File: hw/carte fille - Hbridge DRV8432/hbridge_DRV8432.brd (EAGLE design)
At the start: 50 x 40 mm, 37 parts, among them IC1 DRV8402

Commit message: Start routing the board
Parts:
- moved R1 28.1 mm to (-8.89, 27.9)
- moved C16 18.0 mm to (60.2, 19.6)
- moved C19 17.8 mm to (60.2, 14.0)
- moved R3 17.8 mm to (-11.4, 24.1)
- moved C20 17.7 mm to (59.7, 29.7)
- moved C15 16.9 mm to (58.9, 25.4)
- moved R2 16.1 mm to (-7.87, 20.3), turned to 0 degrees
- moved R11 14.0 mm to (-7.62, 16.5)
- moved C18 14.0 mm to (24.1, 4.57), turned to 270 degrees
- moved R4 8.52 mm to (11.9, 17.3), turned to 225 degrees
- moved R7 7.47 mm to (13.5, 15.7), turned to 225 degrees
- moved R8 6.65 mm to (15.0, 14.2), turned to 225 degrees
- moved C2 6.49 mm to (19.6, 10.7), turned to 270 degrees
- moved C7 5.73 mm to (21.6, 10.7), turned to 270 degrees
- moved R9 4.60 mm to (15.0, 20.8)
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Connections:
- net GND: no longer C15.1, C16.1, C19.1, C20.1
- net GVDD: no longer R1.2, R11.2, R2.2, R3.2
- net N$1: no longer R3.1
- net N$16: now also IC1.P$5; no longer IC1.P$15, R11.1
- net N$17: now also IC1.P$6; no longer IC1.P$4
- net N$18: now also IC1.P$14; no longer IC1.P$6
- net N$19: now also IC1.P$15; no longer IC1.P$14
- net N$6: no longer R2.1
- net N$8: now also IC1.P$4; no longer IC1.P$5, R1.1
- net PVDD: no longer C15.2, C16.2, C19.2, C20.2
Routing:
- net PVDD: track 0.00 -> 96.0 mm, vias 0 -> 4
- net GVDD: track 0.00 -> 83.7 mm
- net N$17: track 0.00 -> 21.9 mm
- net N$16: track 0.00 -> 20.5 mm
- net N$20: track 0.00 -> 20.2 mm
- net N$19: track 0.00 -> 19.4 mm
- net N$8: track 0.00 -> 19.2 mm
- net N$18: track 0.00 -> 18.6 mm
- net N$6: track 0.00 -> 18.4 mm
- net N$1: track 0.00 -> 17.8 mm
- net GND: track 0.00 -> 16.4 mm, vias 0 -> 3
- net OUT_D: track 0.00 -> 10.8 mm
- net N$5: track 0.00 -> 10.4 mm
- net OUT_C: track 0.00 -> 10.0 mm
- net OUT_A: track 0.00 -> 9.84 mm
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- added copper zone on layer 1, net GND
- added copper zone on layer 16, net GND

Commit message: rework board routing
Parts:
- removed C10, C11, C12, C13, C15, C16, C19, C20: 100nF - 0805, resistor:C0805
- removed C14: 100n, etienne:805
- removed C18: 47uF, etienne:E3,5-8
- removed C22: 330µF, etienne:E3,5-8
- removed C5: 10nF - 0805, resistor:C0805
- removed SIGNAL: (no value), con-lsta:FE09
- added C17: 47u, rcl:B/3528-21W
- added C21: 1u, rcl:C0805
- added C31, C32, C33, C34: 100n, rcl:C0805
- added C35, C36, C37, C38: 100n, rcl:C0603
- added H1, H2, H3, H4: MOUNT-HOLE3.2, holes:3,2
- added JP1: (no value), pinhead-2:1X08
- added X4: M1-2, con-wago-500:W237-102
- added X5: M3-4, con-wago-500:W237-102
- added X6: +12V, con-wago-500:W237-102
- added X7: +24V, con-wago-500:W237-102
- C1: value 10nF - 0805 -> 10n; device resistor:C0805 -> rcl:C0805
- C2, C6, C8: value 1uF - 0805 -> 1u; device resistor:C0805 -> rcl:C0805
- C3: value 1000uF -> 1000u; device etienne:E3,5-8 -> rcl:E3,5-10
- C4: value 1000uF -> 100n; device etienne:E3,5-8 -> rcl:C0603K
- C7: value 1uF -0805 -> 1u; device resistor:C0805 -> rcl:C0805
- C9: value 1uF - 0805 -> 330u; device resistor:C0805 -> rcl:B/3528-21W
- R10: value 3R3 - 0603 -> 3.3; device resistor:R0603 -> rcl:R1206
- R12: value 3R3 - 0603 -> (none); device resistor:R0603 -> rcl:R0603
- R9: value 27K - 0603 -> 1; device resistor:R0603 -> rcl:R0603
- moved X1 38.4 mm to (41.1, 19.6), turned to 270 degrees
- moved R12 35.0 mm to (9.04, 18.7)
- moved R5 32.8 mm to (37.6, 18.4), turned to 180 degrees
- moved C9 30.5 mm to (10.2, 27.9)
- moved R6 29.9 mm to (37.6, 23.4), turned to 180 degrees
- moved C4 27.9 mm to (12.8, 19.0), turned to 90 degrees
- moved X2 23.6 mm to (21.9, 31.2), turned to 180 degrees
- moved X3 23.4 mm to (21.9, 7.85), turned to 0 degrees
- moved C8 20.9 mm to (10.0, 11.0)
- moved C2 20.9 mm to (29.8, 28.8), turned to 180 degrees
- moved C6 19.2 mm to (29.6, 10.1), turned to 180 degrees
- moved R11 12.5 mm to (-13.2, 27.7)
- moved R2 10.8 mm to (-15.7, 27.7), turned to 90 degrees
- moved R10 8.00 mm to (34.3, 31.5)
- moved C7 6.93 mm to (14.7, 10.8), turned to 90 degrees
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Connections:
- removed net N$14: C5.1, R12.2
- removed net N$15: C13.1, IC1.P$35
- removed net N$22: R5.1, X1.3
- removed net OUT_A: C13.2, IC1.P$33, X2.1
- removed net OUT_B: C12.2, IC1.P$30, X2.2
- removed net OUT_C: C11.2, IC1.P$25, X3.1
- removed net OUT_D: C10.2, IC1.P$22, X3.2
- new net GND1: X6.1, X7.1
- new net M1A: C33.1, IC1.P$33, X2.1, X4.1
- new net M1B: C32.1, IC1.P$30, X2.2, X4.2
- new net M1C: C31.2, IC1.P$25, X3.1, X5.1
- new net M1D: C34.2, IC1.P$22, X3.2, X5.2
- new net N$25: C33.2, IC1.P$35
- new net N$26: C32.2, IC1.P$28
- new net N$27: C31.1, IC1.P$27
- new net N$28: C34.1, IC1.P$20
- net GND: now also C1.1, C17.-, C2.1, C21.1, C35.1, C36.1, C37.1, C38.1, C6.1, C7.1, C8.1, C9.-, R9.1, X1.4; no longer C1.2, C14.1, C18.-, C2.2, C22.-, C4.-, C5.2, C6.2, C7.2, C8.2, C9.2, IC1.P$9, R4.2, R7.2, R8.2, R9.2, SIGNAL.1, X1.1
- net GVDD: now also C17.+, C2.2, C21.2, C6.2, C7.2, C8.2, C9.+; no longer C18.+, C2.1, C22.+, C6.1, C7.1, C8.1, C9.1
- net N$1: now also JP1.8; no longer SIGNAL.9
- net N$10: now also IC1.P$7, R12.2; no longer C12.1, IC1.P$28
- net N$11: now also C4.1; no longer C14.2
- net N$12: now also X1.2; no longer C10.1, IC1.P$20
- net N$13: now also C1.2, R10.1; no longer C1.1, R10.2
- net N$16: now also JP1.5; no longer SIGNAL.6
- net N$17: now also JP1.4; no longer SIGNAL.5
- net N$18: now also JP1.3; no longer SIGNAL.4
- net N$19: now also JP1.2; no longer SIGNAL.3
- net N$2: now also X1.1, X6.2; no longer X1.2
- net N$20: now also JP1.1; no longer SIGNAL.2
- net N$6: now also JP1.7; no longer SIGNAL.8
- net N$7: now also R5.1, X1.3, X7.2; no longer C11.1, IC1.P$27
- net N$8: now also JP1.6; no longer SIGNAL.7
- net N$9: now also C4.2, IC1.P$9, R12.1, R4.2, R7.2, R8.2, R9.2; no longer IC1.P$7, R9.1
- net PVDD: now also C35.2, C36.2, C37.2, C38.2, R10.2; no longer C4.+, R10.1, R12.1
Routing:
- net PVDD: track 96.0 -> 13.2 mm, vias 4 -> 0
- net N$26: track 0.00 -> 25.4 mm
- net N$27: track 0.00 -> 24.4 mm
- net M1D: track 0.00 -> 20.9 mm
- net M1C: track 0.00 -> 20.8 mm
- net M1B: track 0.00 -> 19.2 mm
- net M1A: track 0.00 -> 18.0 mm
- net OUT_D: track 10.8 -> 0.00 mm
- net N$25: track 0.00 -> 10.6 mm
- net OUT_C: track 10.0 -> 0.00 mm
- net OUT_A: track 9.84 -> 0.00 mm
- net OUT_B: track 9.69 -> 0.00 mm
- net GVDD: track 83.7 -> 91.6 mm
- net N$17: track 21.9 -> 14.1 mm
- net GND: track 16.4 -> 8.88 mm, vias 3 -> 0
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- added copper zone on layer 1, net M1A
- added copper zone on layer 1, net M1B
- added copper zone on layer 1, net M1C
- added copper zone on layer 1, net M1D
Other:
- board size 50 x 40 mm -> 50 x 39 mm

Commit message: wip
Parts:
- removed R5, R6: 0R, resistor:R0603
- moved R9 1.14 mm to (10.1, 19.2)
- moved R12 1.10 mm to (8.05, 19.2)
- moved C4 0.42 mm to (12.5, 18.7)
- moved R10 0.25 mm to (34.1, 31.3)
- moved C37 0.22 mm to (34.1, 13.8), turned to 90 degrees
- moved C1 0.22 mm to (36.4, 33.7)
- moved C36 0.20 mm to (34.1, 25.4), turned to 270 degrees
- moved C38 0.13 mm to (32.0, 13.8), turned to 90 degrees
- turned C35 to 270 degrees
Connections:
- removed net GND1: X6.1, X7.1
- removed net N$2: R6.1, X1.1, X6.2
- removed net N$7: R5.1, X1.3, X7.2
- net GND: now also X6.1, X7.1
- net GVDD: now also X1.1, X6.2; no longer R6.2
- net PVDD: now also X1.3, X7.2; no longer R5.2
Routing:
- net PVDD: track 13.2 -> 67.1 mm
- net GVDD: track 91.6 -> 135.3 mm
- net N$9: track 2.27 -> 19.7 mm, vias 0 -> 1
- net N$28: track 0.00 -> 11.2 mm
- net GND: track 8.88 -> 18.7 mm, vias 0 -> 3
- net N$2: track 9.24 -> 0.00 mm
- net N$7: track 8.01 -> 0.00 mm
- net N$13: track 2.29 -> 3.33 mm
- net N$4: track 6.01 -> 4.99 mm
- net N$3: track 6.60 -> 5.58 mm
- net N$5: track 6.52 -> 5.51 mm
- net N$11: track 2.73 -> 3.55 mm
- net N$10: track 6.63 -> 7.42 mm
- net N$26: track 25.4 -> 24.9 mm
- added copper zone on layer 1, net PVDD
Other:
- board size 50 x 39 mm -> 53.6 x 42 mm

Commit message: finish routing
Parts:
- removed R1, R11, R2, R3: 10K - 0603, resistor:R0603
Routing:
- net M1C: track 20.8 -> 26.9 mm
- net M1B: track 19.2 -> 24.5 mm
- net PVDD: track 67.1 -> 70.1 mm
- net M1A: track 18.0 -> 20.6 mm
- net M1D: track 20.9 -> 22.9 mm
- net GVDD: track 135.3 -> 136.1 mm
- removed copper zone on layer 1, net M1A
- removed copper zone on layer 1, net M1B
- removed copper zone on layer 1, net M1C
- removed copper zone on layer 1, net M1D
- removed copper zone on layer 1, net PVDD

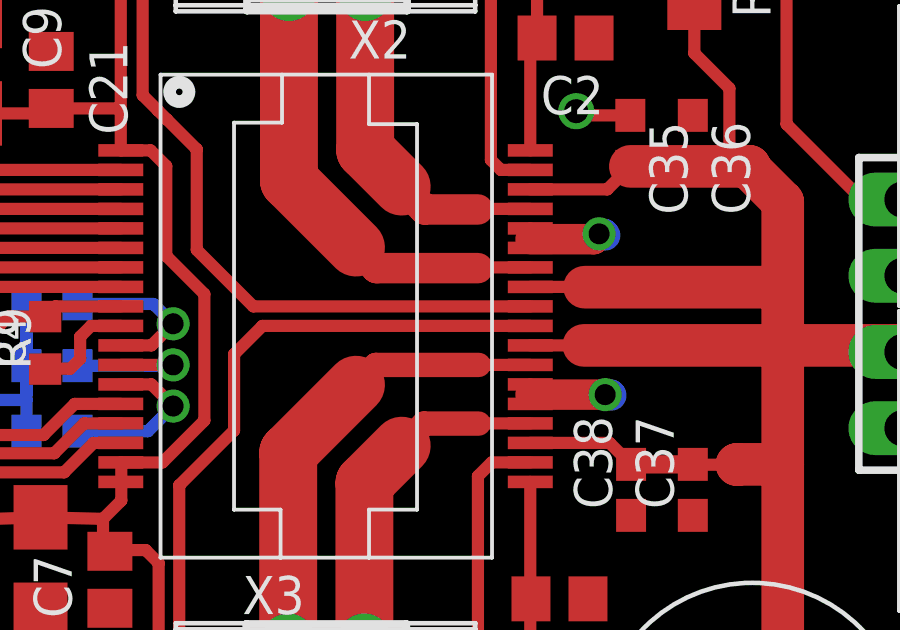
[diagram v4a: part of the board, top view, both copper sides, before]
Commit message: fix power section
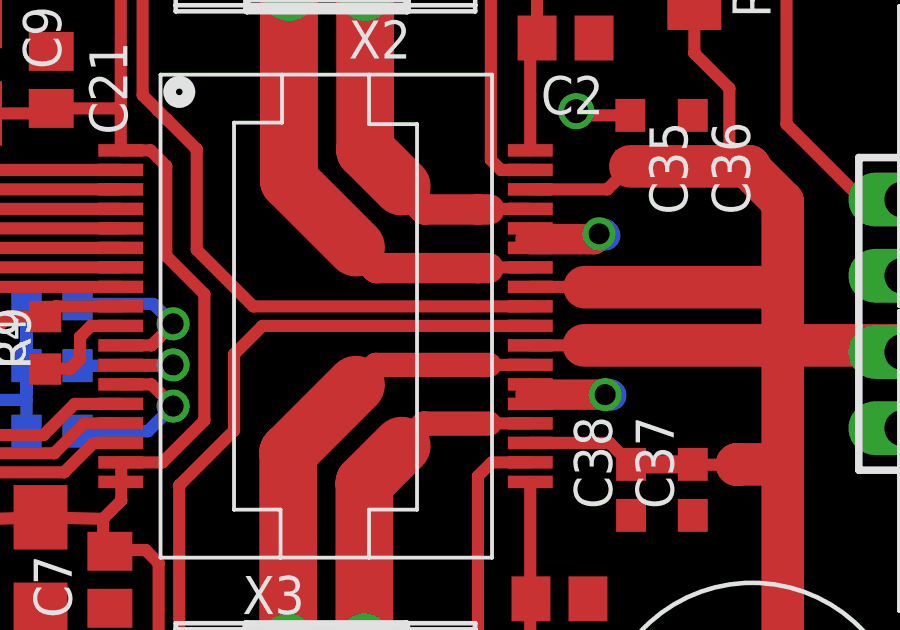
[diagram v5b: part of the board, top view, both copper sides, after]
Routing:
- net M1C: track 26.9 -> 27.6 mm
- net M1B: track 24.5 -> 25.2 mm
- net M1D: track 22.9 -> 23.6 mm
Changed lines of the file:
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@@
 <wire x1="23.1648" y1="31.1912" x2="23.1648" y2="25.0952" width="1.9304" layer="1"/>
 <wire x1="23.1648" y1="25.0952" x2="24.384" y2="23.876" width="1.9304" layer="1"/>
-<wire x1="28.669" y1="23.133" x2="26.943" y2="23.133" width="0.4064" layer="1"/>
-<wire x1="26.943" y1="23.133" x2="26.924" y2="23.114" width="0.4064" layer="1"/>
+<wire x1="27.305" y1="23.114" x2="26.924" y2="23.114" width="1.016" layer="1"/>
 <wire x1="26.924" y1="23.114" x2="25.146" y2="23.114" width="1.016" layer="1"/>
 <wire x1="25.146" y1="23.114" x2="24.384" y2="23.876" width="1.016" layer="1"/>
-<wire x1="27.0002" y1="23.114" x2="27.0002" y2="23.0886" width="0.6096" layer="1"/>
+<wire x1="26.924" y1="23.114" x2="27.0002" y2="23.0886" width="0.6096" layer="1"/>
 <wire x1="27.0002" y1="23.0886" x2="26.9748" y2="23.0632" width="0.6096" layer="1"/>
-<wire x1="27.0002" y1="23.114" x2="26.924" y2="23.114" width="0.6096" layer="1"/>
+<wire x1="28.669" y1="23.133" x2="27.305" y2="23.133" width="0.4064" layer="1"/>
+<wire x1="27.305" y1="23.133" x2="27.305" y2="23.114" width="0.4064" layer="1"/>
 </signal>
 <signal name="M1B">
@@
 <wire x1="20.6248" y1="31.1912" x2="20.6248" y2="24.0792" width="1.9304" layer="1"/>
 <wire x1="20.6248" y1="24.0792" x2="22.86" y2="21.844" width="1.9304" layer="1"/>
-<wire x1="28.669" y1="21.183" x2="26.9488" y2="21.183" width="0.4064" layer="1"/>
-<wire x1="26.9488" y1="21.183" x2="26.924" y2="21.1582" width="0.4064" layer="1"/>
+<wire x1="26.9488" y1="21.183" x2="27.2796" y2="21.1582" width="0.4064" layer="1"/>
+<wire x1="27.2796" y1="21.1582" x2="26.924" y2="21.1582" width="1.016" layer="1"/>
 <wire x1="26.924" y1="21.1582" x2="23.5458" y2="21.1582" width="1.016" layer="1"/>
 <wire x1="23.5458" y1="21.1582" x2="22.86" y2="21.844" width="1.016" layer="1"/>
+<wire x1="28.669" y1="21.183" x2="26.924" y2="21.183" width="0.4064" layer="1"/>
+<wire x1="26.924" y1="21.183" x2="26.924" y2="21.1582" width="0.4064" layer="1"/>
 </signal>
 <signal name="M1C">
@@
 <wire x1="20.5994" y1="15.0114" x2="22.86" y2="17.272" width="1.9304" layer="1"/>
 <wire x1="28.669" y1="17.933" x2="26.95" y2="17.933" width="0.4064" layer="1"/>
-<wire x1="26.95" y1="17.933" x2="26.9494" y2="17.9324" width="0.4064" layer="1"/>
-<wire x1="26.9494" y1="17.9324" x2="23.5204" y2="17.9324" width="0.8128" layer="1"/>
+<wire x1="26.95" y1="17.933" x2="27.305" y2="17.9324" width="0.4064" layer="1"/>
+<wire x1="27.305" y1="17.9324" x2="23.5204" y2="17.9324" width="0.8128" layer="1"/>
 <wire x1="23.5204" y1="17.9324" x2="22.86" y2="17.272" width="0.8128" layer="1"/>
 </signal>
@@
 <wire x1="23.1394" y1="13.9954" x2="24.384" y2="15.24" width="1.9304" layer="1"/>
 <wire x1="28.669" y1="15.983" x2="26.9558" y2="15.983" width="0.4064" layer="1"/>
-<wire x1="26.9558" y1="15.983" x2="26.9494" y2="15.9766" width="0.4064" layer="1"/>
-<wire x1="26.9494" y1="15.9766" x2="25.1206" y2="15.9766" width="0.8128" layer="1"/>
+<wire x1="26.9558" y1="15.983" x2="27.305" y2="15.9766" width="0.4064" layer="1"/>
+<wire x1="27.305" y1="15.9766" x2="25.1206" y2="15.9766" width="0.8128" layer="1"/>
 <wire x1="25.1206" y1="15.9766" x2="24.384" y2="15.24" width="0.8128" layer="1"/>
 </signal>

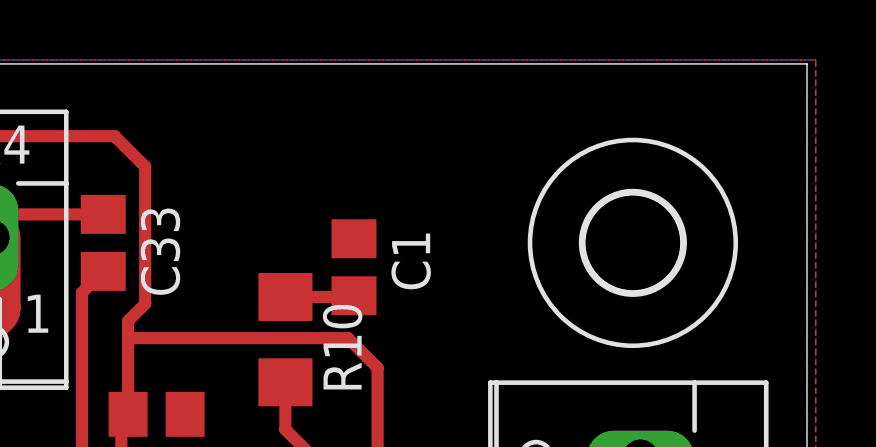
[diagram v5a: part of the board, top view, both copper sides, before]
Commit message: add open hardware logo
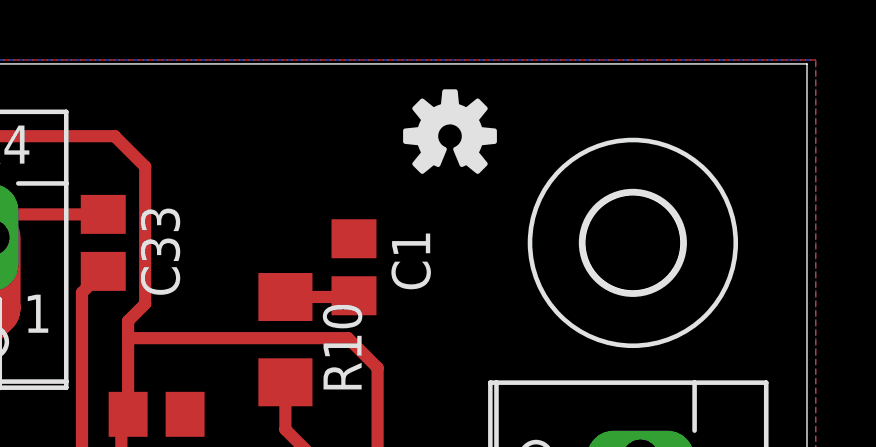
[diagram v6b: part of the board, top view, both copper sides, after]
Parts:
- added U$1: OSHW-LOGOS, SparkFun-Aesthetics:OSHW-LOGO-S
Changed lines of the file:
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@@
 <layer number="19" name="Unrouted" color="6" fill="1" visible="yes" active="yes"/>
 <layer number="20" name="Dimension" color="15" fill="1" visible="yes" active="yes"/>
-<layer number="21" name="tPlace" color="7" fill="1" visible="no" active="yes"/>
-<layer number="22" name="bPlace" color="7" fill="1" visible="no" active="yes"/>
+<layer number="21" name="tPlace" color="7" fill="1" visible="yes" active="yes"/>
+<layer number="22" name="bPlace" color="7" fill="1" visible="yes" active="yes"/>
 <layer number="23" name="tOrigins" color="15" fill="1" visible="yes" active="yes"/>
 <layer number="24" name="bOrigins" color="15" fill="1" visible="yes" active="yes"/>
@@
 <layer number="51" name="tDocu" color="7" fill="1" visible="yes" active="yes"/>
 <layer number="52" name="bDocu" color="7" fill="1" visible="yes" active="yes"/>
+<layer number="53" name="tGND_GNDA" color="7" fill="9" visible="no" active="no"/>
+<layer number="54" name="bGND_GNDA" color="1" fill="9" visible="no" active="no"/>
+<layer number="56" name="wert" color="7" fill="1" visible="no" active="no"/>
 <layer number="91" name="Nets" color="2" fill="1" visible="no" active="no"/>
 <layer number="92" name="Busses" color="1" fill="1" visible="no" active="no"/>
@@
 <layer number="99" name="SpiceOrder" color="5" fill="1" visible="no" active="no"/>
 <layer number="100" name="Muster" color="7" fill="1" visible="no" active="no"/>
+<layer number="101" name="Cutout" color="7" fill="1" visible="no" active="yes"/>
+<layer number="102" name="NoBridge" color="7" fill="1" visible="no" active="yes"/>
+<layer number="103" name="tMap" color="7" fill="1" visible="no" active="yes"/>
+<layer number="104" name="Name" color="16" fill="1" visible="no" active="yes"/>
+<layer number="105" name="tPlate" color="7" fill="1" visible="no" active="yes"/>
+<layer number="106" name="bPlate" color="7" fill="1" visible="no" active="yes"/>
+<layer number="107" name="Crop" color="7" fill="1" visible="no" active="yes"/>
+<layer number="116" name="Patch_BOT" color="9" fill="4" visible="no" active="yes"/>
+<layer number="120" name="DimPTH" color="7" fill="1" visible="no" active="yes"/>
+<layer number="121" name="_tsilk" color="7" fill="1" visible="no" active="yes"/>
+<layer number="122" name="_bsilk" color="7" fill="1" visible="no" active="yes"/>
+<layer number="125" name="_tNames" color="7" fill="1" visible="no" active="yes"/>
+<layer number="144" name="Drill_legend" color="7" fill="1" visible="no" active="yes"/>
+<layer number="151" name="HeatSink" color="7" fill="1" visible="no" active="yes"/>
+<layer number="200" name="200bmp" color="7" fill="1" visible="no" active="yes"/>
+<layer number="201" name="Tech2" color="7" fill="1" visible="no" active="yes"/>
+<layer number="202" name="Ref" color="7" fill="1" visible="no" active="yes"/>
+<layer number="203" name="203bmp" color="4" fill="10" visible="yes" active="yes"/>
+<layer number="204" name="204bmp" color="5" fill="10" visible="yes" active="yes"/>
+<layer number="205" name="205bmp" color="6" fill="10" visible="yes" active="yes"/>
+<layer number="206" name="206bmp" color="7" fill="10" visible="yes" active="yes"/>
+<layer number="207" name="207bmp" color="8" fill="10" visible="yes" active="yes"/>
+<layer number="208" name="208bmp" color="9" fill="10" visible="yes" active="yes"/>
+<layer number="209" name="209bmp" color="10" fill="10" visible="yes" active="yes"/>
+<layer number="210" name="210bmp" color="11" fill="10" visible="yes" active="yes"/>
+<layer number="211" name="211bmp" color="12" fill="10" visible="yes" active="yes"/>
+<layer number="212" name="212bmp" color="13" fill="10" visible="yes" active="yes"/>
+<layer number="213" name="213bmp" color="14" fill="10" visible="yes" active="yes"/>
+<layer number="214" name="214bmp" color="15" fill="10" visible="yes" active="yes"/>
+<layer number="215" name="215bmp" color="16" fill="10" visible="yes" active="yes"/>
+<layer number="216" name="216bmp" color="7" fill="1" visible="no" active="yes"/>
+<layer number="217" name="217bmp" color="18" fill="1" visible="no" active="no"/>
+<layer number="218" name="218bmp" color="19" fill="1" visible="no" active="no"/>
+<layer number="219" name="219bmp" color="20" fill="1" visible="no" active="no"/>
+<layer number="220" name="220bmp" color="21" fill="1" visible="no" active="no"/>
+<layer number="221" name="221bmp" color="22" fill="1" visible="no" active="no"/>
+<layer number="222" name="222bmp" color="23" fill="1" visible="no" active="no"/>
+<layer number="223" name="223bmp" color="24" fill="1" visible="no" active="no"/>
+<layer number="224" name="224bmp" color="25" fill="1" visible="no" active="no"/>
 <layer number="250" name="Descript" color="3" fill="1" visible="no" active="no"/>
 <layer number="251" name="SMDround" color="12" fill="11" visible="no" active="no"/>
+<layer number="254" name="cooling" color="7" fill="1" visible="no" active="yes"/>
 </layers>
 <board>
@@
 <element name="X6" library="con-wago-500" package="W237-102" value="+12V" x="44.704" y="24.892" rot="R90"/>
 <element name="X7" library="con-wago-500" package="W237-102" value="+24V" x="44.704" y="14.732" rot="R90"/>
+<element name="U$1" library="SparkFun-Aesthetics" package="OSHW-LOGO-S" value="OSHW-LOGOS" x="39.624" y="38.1"/>
 </elements>
 <signals>
